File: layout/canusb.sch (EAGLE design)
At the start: 16 parts, among them IC1 PIC18F2580-E/SO, J1 J_USB_MICROAB_HIROSE_ZX62-AB-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

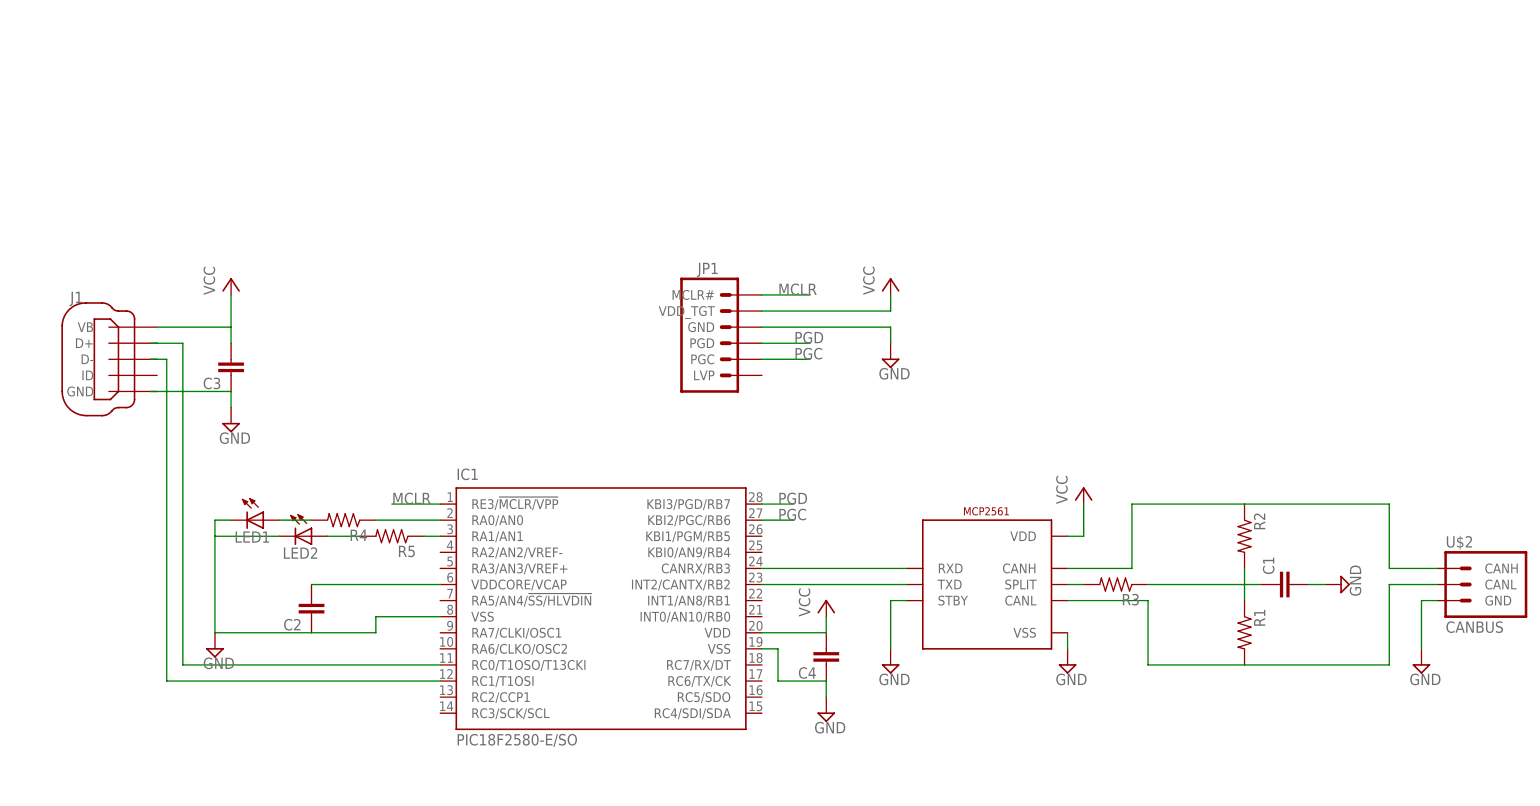
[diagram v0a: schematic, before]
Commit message: schematic and library update
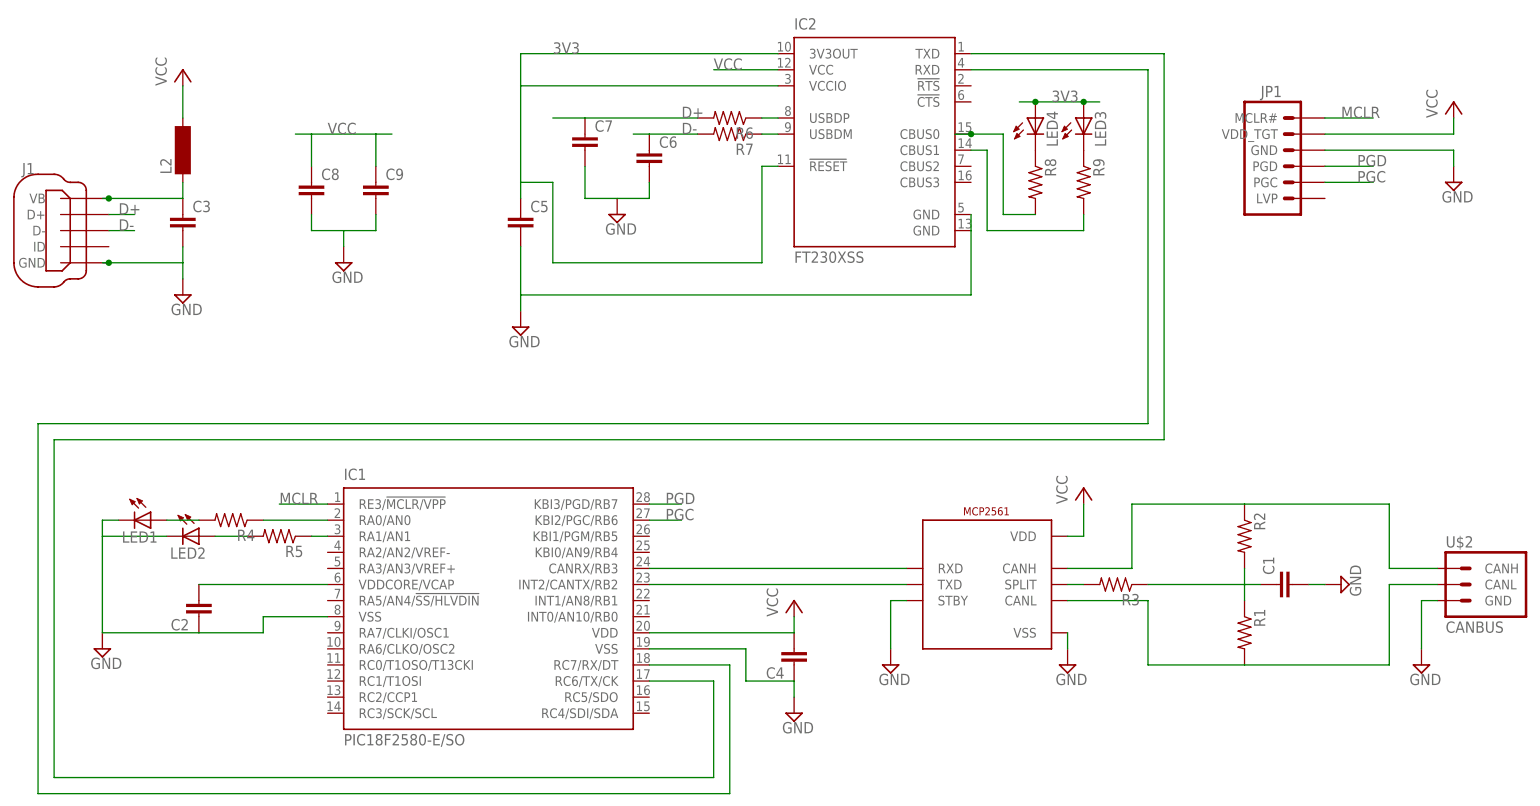
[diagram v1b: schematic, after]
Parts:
- added C5, C6, C7, C8, C9: (no value), rcl:C-EUC0805K
- added IC2: FT230XSS, Canaconda:FT230XSS
- added L2: (no value), Canaconda:FERRITE_BEAD
- added LED3, LED4: (no value), led:LEDCHIPLED_0805
- added R6, R7, R8, R9: (no value), rcl:R-US_M0805
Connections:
- removed net N$8: IC1.RC1/T1OSI, J1.D-
- new net 3V3: C5.1, IC2.!RESET, IC2.3V3OUT, IC2.VCCIO, LED3.A, LED4.A
- new net D+: C7.1, J1.D+, R6.2
- new net D-: C6.1, J1.D-, R7.2
- new net N$15: IC1.RC6/TX/CK, IC2.TXD
- new net N$17: IC2.USBDP, R6.1
- new net N$18: IC2.USBDM, R7.1
- new net N$20: LED4.C, R8.1
- new net N$21: LED3.C, R9.1
- new net N$22: IC2.CBUS0, R8.2
- new net N$23: IC2.CBUS1, R9.2
- new net N$9: C3.1, J1.VB, L2.1
- net GND: now also C3.2, C5.2, C6.2, C7.2, C8.2, C9.2, IC2.GND, IC2.GND@1; no longer C3.1
- net N$5: now also IC1.RC7/RX/DT, IC2.RXD; no longer IC1.RC0/T1OSO/T13CKI, J1.D+
- net VCC: now also C8.1, C9.1, IC2.VCC, L2.2; no longer C3.2, J1.VB
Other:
- moved on the sheet: C2, C3, C4, IC1, J1, JP1, LED1, LED2, R4, R5
